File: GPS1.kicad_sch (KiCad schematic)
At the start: 12 parts, among them J8 GPS_ANT_1, U5 NEO-6M-GPS, U6 24AA32A-I_ST

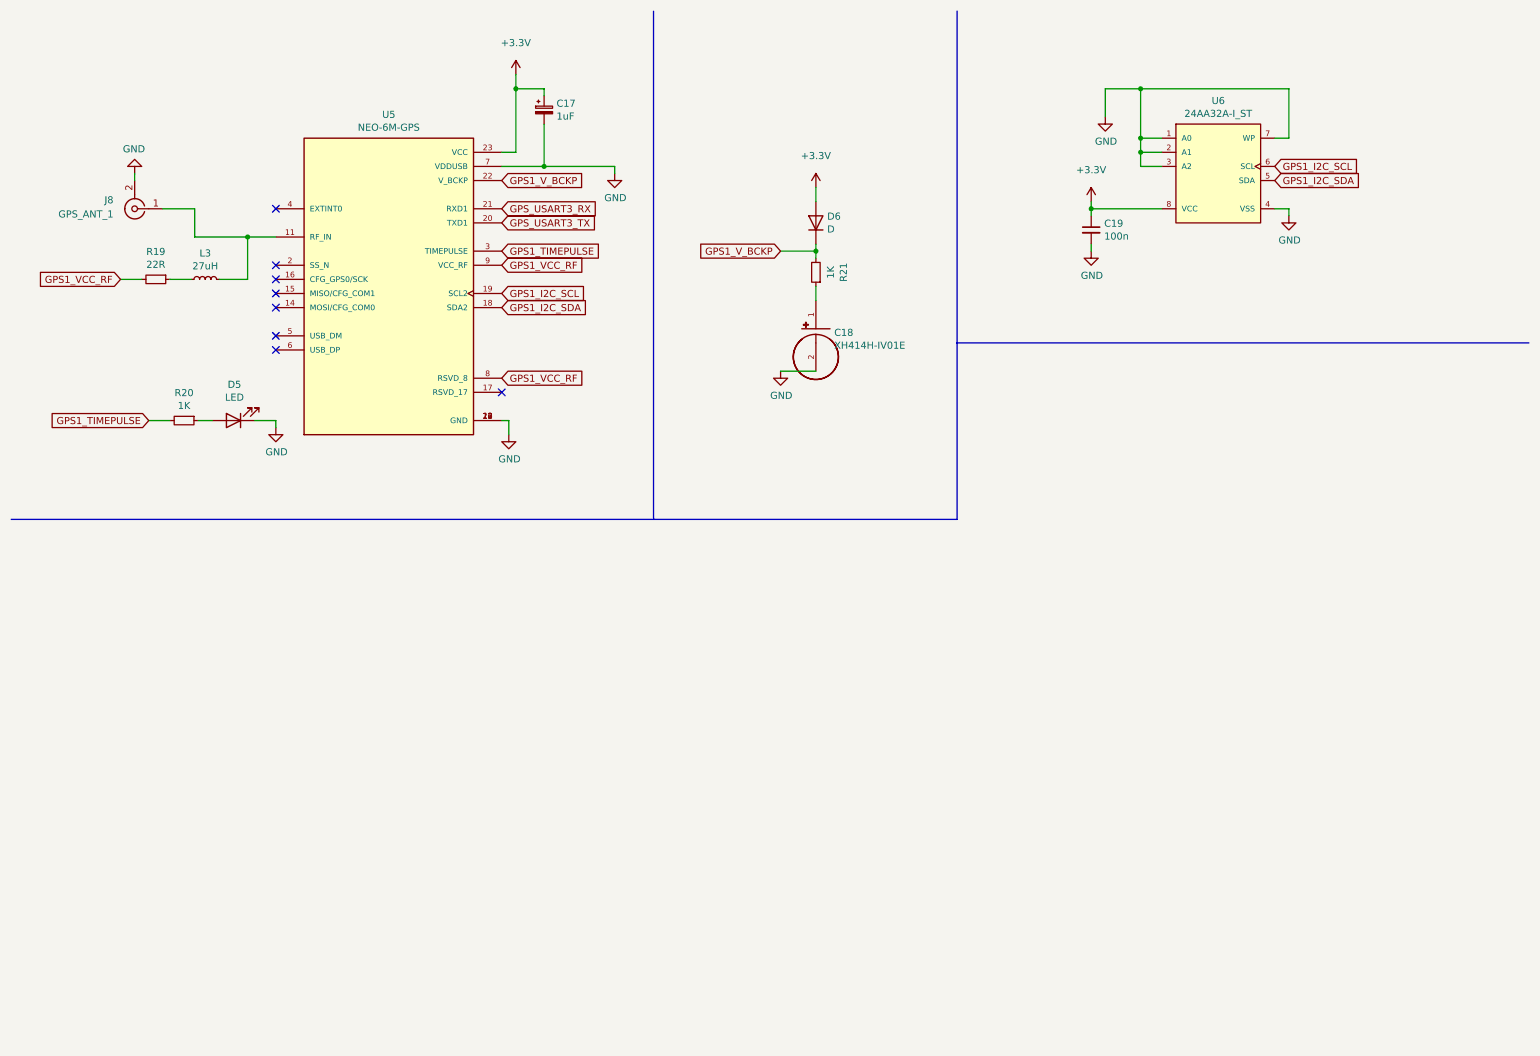
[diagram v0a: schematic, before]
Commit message: Adding M10
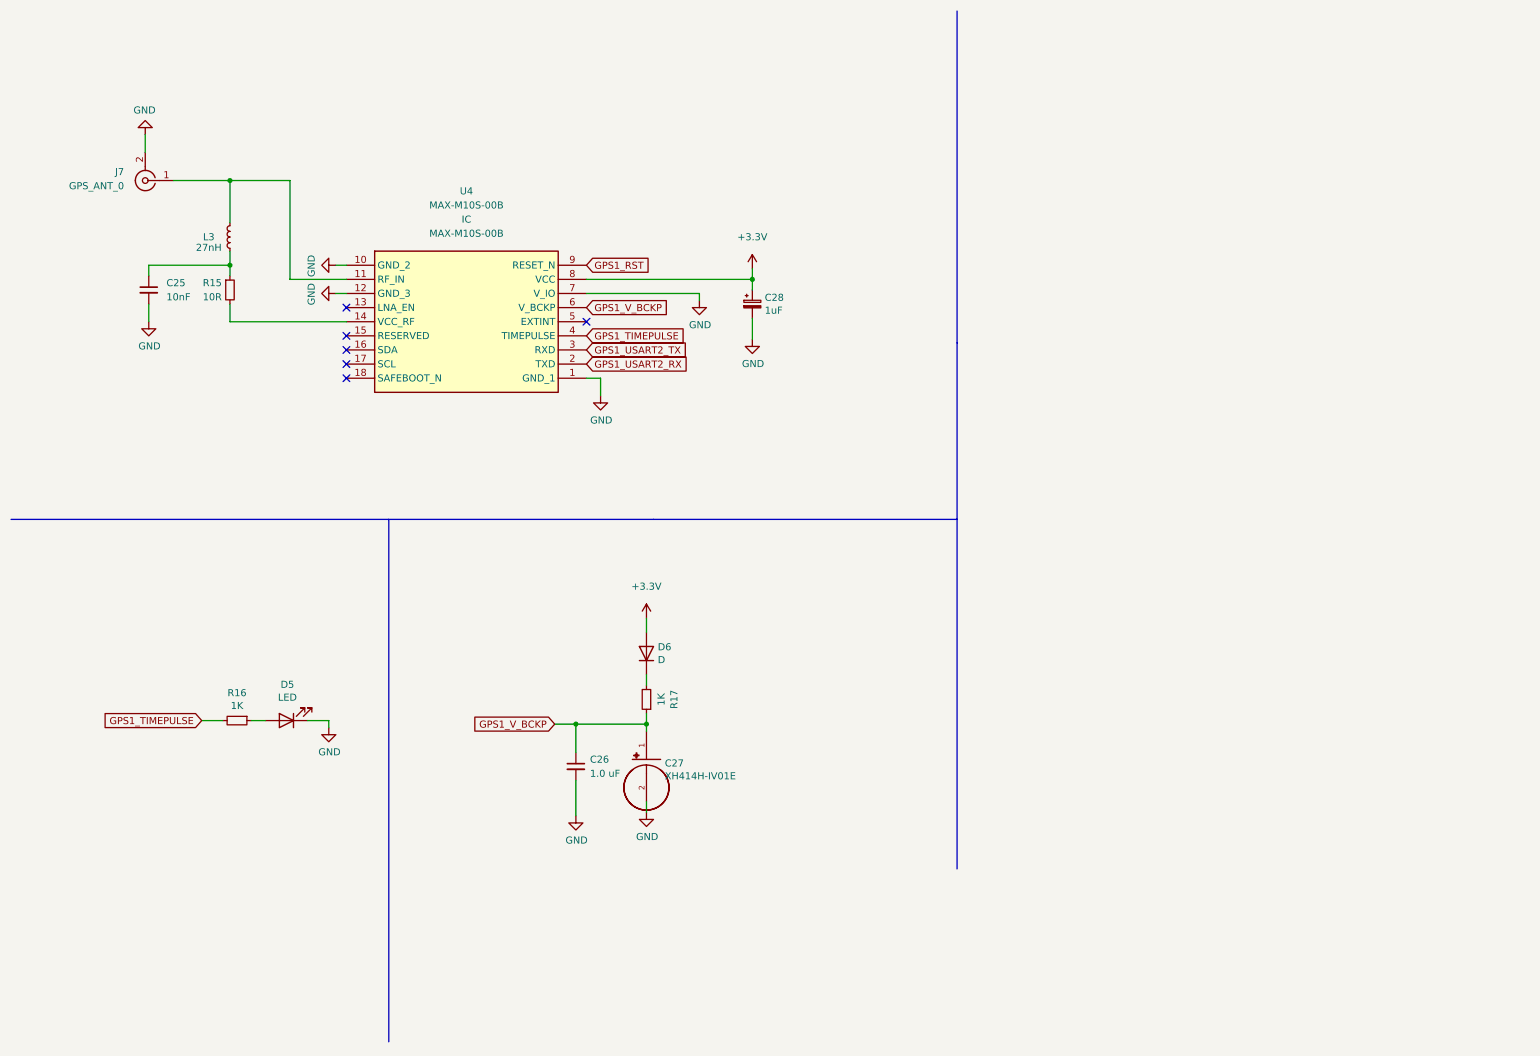
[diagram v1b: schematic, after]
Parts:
- removed C17: 1uF, Capacitor_Tantalum_SMD:CP_EIA-3528-21_Kemet-B_Pad1.50x2.35mm_HandSolder, symbol Device:CP_Small
- removed C18: XH414H-IV01E, XH414H:CAP_XH414H-IV01E, symbol XH414H-IV01E:XH414H-IV01E
- removed C19: 100n, Capacitor_SMD:C_0402_1005Metric, symbol Device:C_Small
- removed J8: GPS_ANT_1, Connector_Coaxial:SMA_Samtec_SMA-J-P-X-ST-EM1_EdgeMount, symbol Connector:Conn_Coaxial
- removed R19: 22R, Resistor_SMD:R_0805_2012Metric, symbol Device:R_Small
- removed R20, R21: 1K, Resistor_SMD:R_0805_2012Metric, symbol Device:R_Small
- removed U5: NEO-6M-GPS, NEO 6M:XCVR_NEO-6M-GPS, symbol NEO-6M-GPS:NEO-6M-GPS
- removed U6: 24AA32A-I_ST, 24AA32 IST:Microchip-24AA32A-I_ST-Level_B, symbol eec:24AA32A-I_ST
- added C25: 10nF, Capacitor_SMD:C_0805_2012Metric, symbol Device:C_Small
- added C26: 1.0 uF, Capacitor_SMD:C_0805_2012Metric, symbol Device:C_Small
- added C27: XH414H-IV01E, XH414H:CAP_XH414H-IV01E, symbol XH414H-IV01E:XH414H-IV01E
- added C28: 1uF, Capacitor_Tantalum_SMD:CP_EIA-3528-21_Kemet-B_Pad1.50x2.35mm_HandSolder, symbol Device:CP_Small
- added J7: GPS_ANT_0, Connector_Coaxial:SMA_Samtec_SMA-J-P-X-ST-EM1_EdgeMount, symbol Connector:Conn_Coaxial
- added R15: 10R, Resistor_SMD:R_0805_2012Metric, symbol Device:R_Small
- added R16, R17: 1K, Resistor_SMD:R_0805_2012Metric, symbol Device:R_Small
- added U4: MAX-M10S-00B, MAX-M10S-00B:MAXM10S00B, symbol MAX-M10S-00B:MAX-M10S-00B
- L3: value 27uH -> 27nH
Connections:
- net +3.3V: now also C28.1, U4.8 (VCC)
- net GND: now also C25.2, C26.2, C27.2, C28.2, J7.2 (Ext), U4.1 (GND_1), U4.10 (GND_2), U4.12 (GND_3), U4.7 (V_IO)
- net GPS1_TIMEPULSE: now also R16.2, U4.4 (TIMEPULSE)
- net GPS1_V_BCKP: now also C26.1, C27.1, R17.1, U4.6 (V_BCKP); no longer D6.1 (K)
- net at D5.2 (A): now also R16.1
- net at L3.1: now also C25.1, R15.1
- net at L3.2: now also J7.1 (In), U4.11 (RF_IN)
- new net: D6.1 (K), R17.2
- new net: R15.2, U4.14 (VCC_RF)
- new net GPS1_RST: U4.9 (RESET_N)
- new net GPS1_USART2_RX: U4.2 (TXD)
- new net GPS1_USART2_TX: U4.3 (RXD)
- no-connect marks 8 -> 6

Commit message: Finished M10
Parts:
- C25: footprint Capacitor_SMD:C_0805_2012Metric -> Capacitor_SMD:C_0402_1005Metric
- L3: footprint Inductor_SMD:L_0805_2012Metric -> Inductor_SMD:L_0402_1005Metric
- R15: footprint Resistor_SMD:R_0805_2012Metric -> Resistor_SMD:R_0402_1005Metric
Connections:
- net GPS1_RST renamed GPS1_RESET
- net GPS1_USART2_RX renamed GPS1_USART3_RX
- net GPS1_USART2_TX renamed GPS1_USART3_TX
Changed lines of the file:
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@@
     (stroke (width 0) (type default) (color 0 0 0 0))
   )
-  (global_label "GPS1_RST" (shape input) (at 115.57 57.785 0) (fields_autoplaced)
-    (effects (font (size 1.27 1.27)) (justify left))
-    (property "Intersheet References" "${INTERSHEET_REFS}" (id 0) (at 127.3569 57.7056 0)
-      (effects (font (size 1.27 1.27)) (justify left) hide)
-    )
-  )
-  (global_label "GPS1_USART2_RX" (shape input) (at 115.57 75.565 0) (fields_autoplaced)
+  (global_label "GPS1_USART3_RX" (shape input) (at 115.57 75.565 0) (fields_autoplaced)
     (effects (font (size 1.27 1.27)) (justify left))
     (property "Intersheet References" "${INTERSHEET_REFS}" (id 0) (at 134.4326 75.4856 0)
@@
     )
   )
-  (global_label "GPS1_USART2_TX" (shape input) (at 115.57 73.025 0) (fields_autoplaced)
+  (global_label "GPS1_USART3_TX" (shape input) (at 115.57 73.025 0) (fields_autoplaced)
     (effects (font (size 1.27 1.27)) (justify left))
     (property "Intersheet References" "${INTERSHEET_REFS}" (id 0) (at 134.1302 72.9456 0)
@@
     )
   )
+  (global_label "GPS1_RESET" (shape input) (at 115.57 57.785 0) (fields_autoplaced)
+    (effects (font (size 1.27 1.27)) (justify left))
+    (property "Intersheet References" "${INTERSHEET_REFS}" (id 0) (at 129.655 57.7056 0)
+      (effects (font (size 1.27 1.27)) (justify left) hide)
+    )
+  )
   (symbol (lib_id "power:GND") (at 69.215 140.97 0) (unit 1)
     (in_bom yes) (on_board yes)
@@
     (property "Reference" "R15" (id 0) (at 48.26 60.96 0))
     (property "Value" "10R" (id 1) (at 48.26 63.5 0))
-    (property "Footprint" "Resistor_SMD:R_0805_2012Metric" (id 2) (at 51.435 62.23 0)
+    (property "Footprint" "Resistor_SMD:R_0402_1005Metric" (id 2) (at 51.435 62.23 0)
       (effects (font (size 1.27 1.27)) hide)
     )
@@
       (effects (font (size 1.27 1.27)) (justify left))
     )
-    (property "Footprint" "Capacitor_SMD:C_0805_2012Metric" (id 2) (at 36.83 62.23 0)
+    (property "Footprint" "Capacitor_SMD:C_0402_1005Metric" (id 2) (at 36.83 62.23 0)
       (effects (font (size 1.27 1.27)) hide)
     )
@@
     (property "Reference" "L3" (id 0) (at 47.625 52.705 0))
     (property "Value" "27nH" (id 1) (at 47.625 54.61 0))
-    (property "Footprint" "Inductor_SMD:L_0805_2012Metric" (id 2) (at 51.435 52.705 0)
-      (effects (font (size 1.27 1.27)) hide)
-    )
+    (property "Footprint" "Inductor_SMD:L_0402_1005Metric" (id 2) (at 51.435 52.705 0)
+      (effects (font (size 1.27 1.27)) hide)
+    )

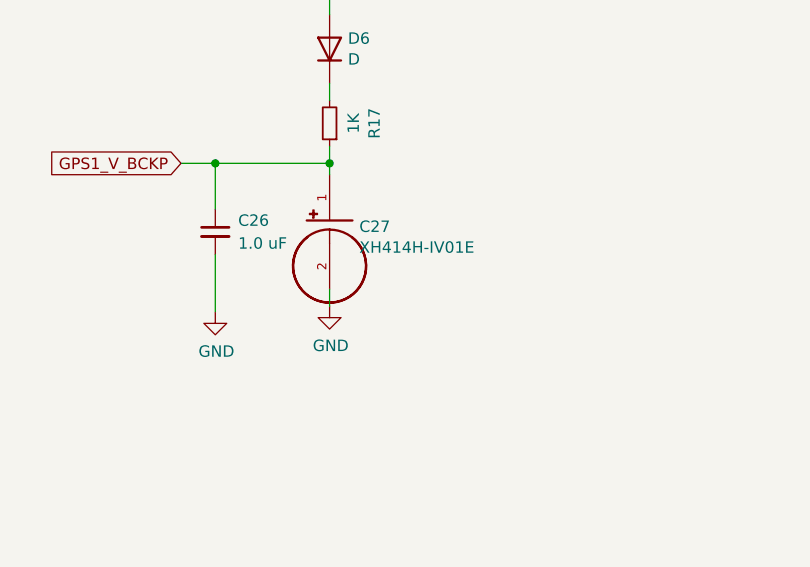
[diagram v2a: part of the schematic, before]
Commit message: Corrected battery position
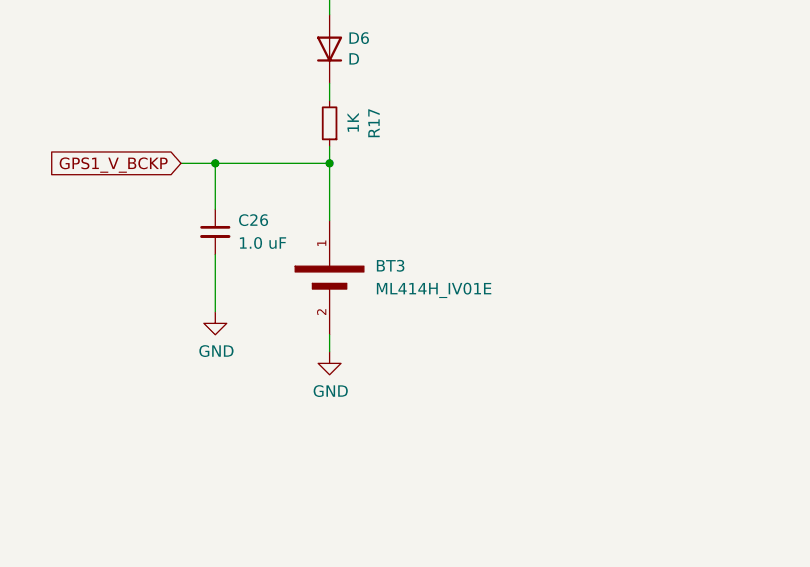
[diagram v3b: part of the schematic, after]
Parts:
- removed C27: XH414H-IV01E, XH414H:CAP_XH414H-IV01E, symbol XH414H-IV01E:XH414H-IV01E
- added BT3: ML414H_IV01E, ML414H_IV01E:SEIKO_ML414H_IV01E, symbol ML414H_IV01E:ML414H_IV01E
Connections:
- net GND: now also BT3.2
- net GPS1_V_BCKP: now also BT3.1
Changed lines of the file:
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@@
     (stroke (width 0) (type default) (color 0 0 0 0))
   )
-  (wire (pts (xy 126.365 154.305) (xy 126.365 156.21))
-    (stroke (width 0) (type default) (color 0 0 0 0))
-  )
-  (wire (pts (xy 126.365 140.335) (xy 126.365 141.605))
+  (wire (pts (xy 126.365 159.385) (xy 126.365 161.29))
+    (stroke (width 0) (type default) (color 0 0 0 0))
+  )
+  (wire (pts (xy 126.365 140.335) (xy 126.365 146.685))
     (stroke (width 0) (type default) (color 0 0 0 0))
   )
@@
     (pin "2")
   )
-  (symbol (lib_id "XH414H-IV01E:XH414H-IV01E") (at 126.365 146.685 0) (unit 1)
-    (in_bom yes) (on_board yes)
-    (property "Reference" "C27" (id 0) (at 129.667 147.3708 0)
-      (effects (font (size 1.27 1.27)) (justify left))
-    )
-    (property "Value" "XH414H-IV01E" (id 1) (at 129.667 149.6822 0)
-      (effects (font (size 1.27 1.27)) (justify left))
-    )
-    (property "Footprint" "XH414H:CAP_XH414H-IV01E" (id 2) (at 126.365 146.685 0)
-      (effects (font (size 1.27 1.27)) (justify left bottom) hide)
-    )
-    (property "Datasheet" "" (id 3) (at 126.365 146.685 0)
-      (effects (font (size 1.27 1.27)) (justify left bottom) hide)
-    )
-    (property "MANUFACTURER" "Seiko" (id 4) (at 126.365 146.685 0)
-      (effects (font (size 1.27 1.27)) (justify left bottom) hide)
-    )
-    (pin "1")
-    (pin "2")
-  )
   (symbol (lib_id "power:GND") (at 70.485 57.785 270) (unit 1)
     (in_bom yes) (on_board yes)
@@
     )
     (pin "1")
+  )
+  (symbol (lib_id "ML414H_IV01E:ML414H_IV01E") (at 126.365 151.765 270) (unit 1)
+    (in_bom yes) (on_board yes) (fields_autoplaced)
+    (property "Reference" "BT3" (id 0) (at 131.445 151.7649 90)
+      (effects (font (size 1.27 1.27)) (justify left))
+    )
+    (property "Value" "ML414H_IV01E" (id 1) (at 131.445 154.3049 90)
+      (effects (font (size 1.27 1.27)) (justify left))
+    )
+    (property "Footprint" "ML414H_IV01E:SEIKO_ML414H_IV01E" (id 2) (at 126.365 151.765 0)
+      (effects (font (size 1.27 1.27)) (justify bottom) hide)
+    )
+    (property "Datasheet" "" (id 3) (at 126.365 151.765 0)
+      (effects (font (size 1.27 1.27)) hide)
+    )
+    (property "STANDARD" "Manufacturer Recommendation" (id 4) (at 126.365 151.765 0)
+      (effects (font (size 1.27 1.27)) (justify bottom) hide)
+    )
+    (property "MANUFACTURER" "SEIKO" (id 5) (at 126.365 151.765 0)
+      (effects (font (size 1.27 1.27)) (justify bottom) hide)
+    )
+    (pin "1")
+    (pin "2")
   )
   (symbol (lib_id "power:GND") (at 118.11 81.28 0) (unit 1)
@@
     (pin "2")
   )
-  (symbol (lib_id "power:GND") (at 126.365 156.21 0) (unit 1)
-    (in_bom yes) (on_board yes)
-    (property "Reference" "#PWR034" (id 0) (at 126.365 162.56 0)
-      (effects (font (size 1.27 1.27)) hide)
-    )
-    (property "Value" "GND" (id 1) (at 126.492 160.6042 0))
-    (property "Footprint" "" (id 2) (at 126.365 156.21 0)
-      (effects (font (size 1.27 1.27)) hide)
-    )
-    (property "Datasheet" "" (id 3) (at 126.365 156.21 0)
-      (effects (font (size 1.27 1.27)) hide)
-    )
+  (symbol (lib_id "power:GND") (at 126.365 161.29 0) (unit 1)
+    (in_bom yes) (on_board yes)
+    (property "Reference" "#PWR034" (id 0) (at 126.365 167.64 0)
+      (effects (font (size 1.27 1.27)) hide)
+    )
+    (property "Value" "GND" (id 1) (at 126.492 165.6842 0))
+    (property "Footprint" "" (id 2) (at 126.365 161.29 0)
+      (effects (font (size 1.27 1.27)) hide)
+    )
+    (property "Datasheet" "" (id 3) (at 126.365 161.29 0)
+      (effects (font (size 1.27 1.27)) hide)
+    )

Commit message: Last commit
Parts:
- removed D6: D, Diode_SMD:D_1206_3216Metric_Pad1.42x1.75mm_HandSolder, symbol Device:D
- added D4: B0520LW-7-F, B0520LW-7-F:SOD3716X145N, symbol B0520LW-7-F:B0520LW-7-F
- C28: value 1uF -> 10uF; footprint Capacitor_Tantalum_SMD:CP_EIA-3528-21_Kemet-B_Pad1.50x2.35mm_HandSolder -> Capacitor_SMD:C_1210_3225Metric
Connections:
- net +3.3V: now also U4.7 (V_IO), D4.2 (A)
- net GND: no longer U4.7 (V_IO)
- net at R17.2: now also D4.1 (K)
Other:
- moved on the sheet: BT3, C25, C26, C28, J7, L3, R15, R17, U4

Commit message: Second commit
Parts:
- removed C26: 1.0 uF, Capacitor_SMD:C_0805_2012Metric, symbol Device:C_Small
- removed C28: 10uF, Capacitor_SMD:C_1210_3225Metric, symbol Device:CP_Small
- removed J7: GPS_ANT_0, Connector_Coaxial:SMA_Samtec_SMA-J-P-X-ST-EM1_EdgeMount, symbol Connector:Conn_Coaxial
- removed U4: MAX-M10S-00B, MAX-M10S-00B:MAXM10S00B, symbol MAX-M10S-00B:MAX-M10S-00B
- added C22: 100nF, Capacitor_SMD:C_0402_1005Metric, symbol Device:C_Small
- added C23: 1uF, Capacitor_SMD:C_1210_3225Metric, symbol Device:C_Small
- added C24: 10uF, Capacitor_SMD:C_1210_3225Metric, symbol Device:C_Small
- added C9: 1.0 uF, Capacitor_SMD:C_0805_2012Metric, symbol Device:C_Small
- added IC2: 24AA32A-I_ST, 24AA32A-I_ST:SOP65P640X120-8N, symbol 24AA32A-I_ST:24AA32A-I_ST
- added J3: GPS_ANT_0, Connector_Coaxial:SMA_Samtec_SMA-J-P-H-ST-EM1_EdgeMount, symbol Connector:Conn_Coaxial
- added R18: 10K, Resistor_SMD:R_0402_1005Metric, symbol Device:R_Small
- added R19, R20: 4.7K, Resistor_SMD:R_0402_1005Metric, symbol Device:R_Small
- added U2: NEO-M9N, NEO-M9N:XCVR_NEO-M9N, symbol NEO-M9N:NEO-M9N
- BT3: footprint ML414H_IV01E:SEIKO_ML414H_IV01E -> ML414H IV01E:SEIKO_ML414H_IV01E
- C25: value 10nF -> 100n
- R15: value 10R -> 1K; footprint Resistor_SMD:R_0402_1005Metric -> Resistor_SMD:R_0805_2012Metric
- R16: value 1K -> 10R; footprint Resistor_SMD:R_0805_2012Metric -> Resistor_SMD:R_0402_1005Metric
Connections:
- net +3.3V: now also C25.1, C23.1, C24.1, IC2.8 (VCC), R18.2, R19.1, R20.1, U2.23 (VCC)
- net GND: now also C22.2, C23.2, C24.2, C9.2, IC2.1 (A0), IC2.2 (A1), IC2.3 (A2), IC2.4 (VSS), IC2.7 (WP), J3.2 (Ext), U2.10 (GND), U2.12 (GND), U2.13 (GND), U2.24 (GND)
- net GPS1_RESET: now also U2.8 (RESET_N)
- net GPS1_TIMEPULSE: now also R17.2, U2.3 (TIMEPULSE); no longer R16.2
- net GPS1_V_BCKP: now also R15.1, C9.1, U2.22 (V_BCKP); no longer R17.1
- net at R16.1: now also L3.1, C22.1; no longer D5.2 (A)
- net at R15.2: now also D4.1 (K)
- net at L3.2: now also J3.1 (In), U2.11 (RF_IN)
- new net: D5.2 (A), R17.1
- new net: U2.15 (RESERVED), U2.16 (RESERVED), U2.17 (RESERVED)
- new net GPS1_D_SEL: R18.1, U2.2 (D_SEL)
- new net GPS1_I2C_SCL: IC2.6 (SCL), R20.2, U2.19 (SCL/SPI_CLK)
- new net GPS1_I2C_SDA: IC2.5 (SDA), R19.2, U2.18 (SDA/SPI_CS_N)
- new net GPS1_RF: R16.2, U2.9 (VCC_RF)
- new net GPS1_USART2_RX: U2.20 (TXD/SPI_MISO)
- new net GPS1_USART2_TX: U2.21 (RXD/SPI_MOSI)
